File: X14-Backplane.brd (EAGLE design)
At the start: 88.9 x 139.7 mm, 34 parts, among them J2 PXC-PTSM-04-RA-1778641, J3 PXC-8-RA-1778683, J8 PXC-8-RA-1778683

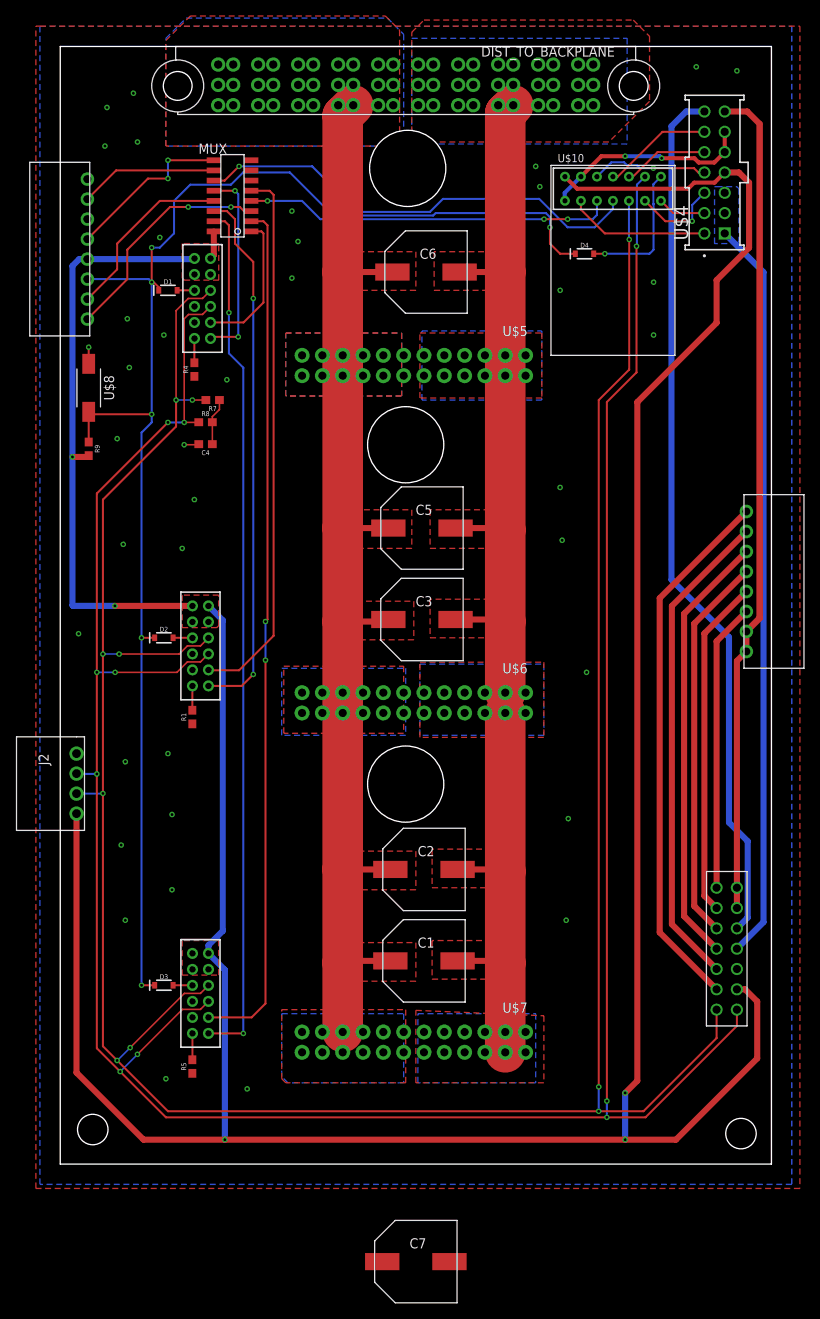
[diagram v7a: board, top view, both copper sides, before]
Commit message: Added Silkscreen, last cap
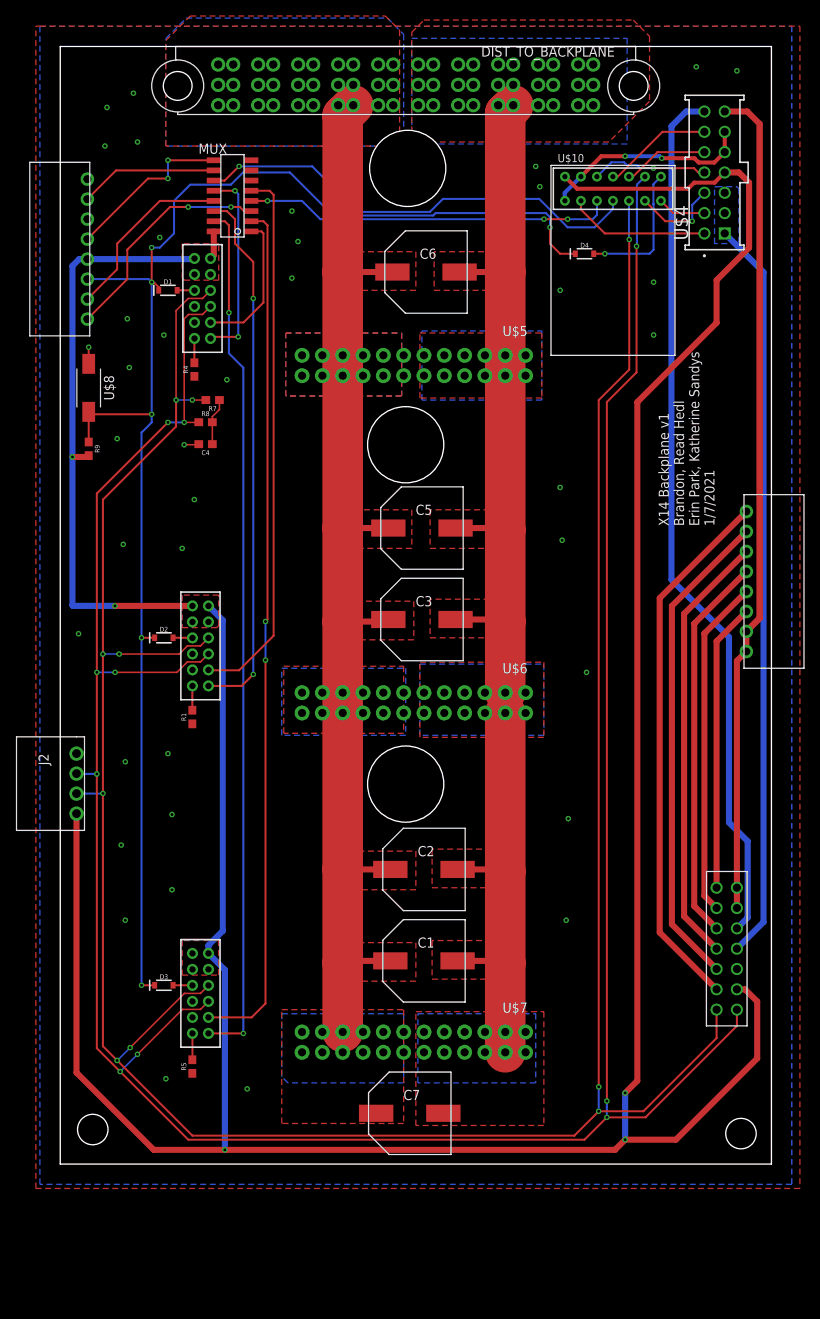
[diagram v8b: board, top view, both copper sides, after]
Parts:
- moved C7 18.6 mm to (43.7, 6.35)
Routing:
- net CAN_H: track 340.3 -> 342.8 mm
- net 3V3: track 434.3 -> 436.6 mm
- net CAN_L: track 344.7 -> 347.0 mm
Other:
- board text added: "X14 Backplane v1 Brandon, Read Hedl Erin Park, Katherine Sandys 1/7/2021"
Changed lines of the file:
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@@
 <hole x="43.18" y="89.916" drill="9.525"/>
 <hole x="43.434" y="124.46" drill="9.525"/>
+<text x="81.788" y="79.756" size="1.27" layer="25" rot="R90">X14 Backplane v1
+Brandon, Read Hedl
+Erin Park, Katherine Sandys
+1/7/2021</text>
 </plain>
 <attributes>
@@
 <attribute name="VALUE" x="45.72" y="108.966" size="1.27" layer="27" align="center"/>
 </element>
-<element name="C7" library="CAP, aluminin-capacitor-brick-UCM1H331MNL1GS" package="CAPAE1030X1050N" package3d_urn="urn:adsk.eagle:package:24202090/2" value="330uF" x="44.45" y="-12.192" smashed="yes">
-<attribute name="ARROW_PART_NUMBER" value="UCM1H331MNL1GS" x="44.45" y="-12.192" size="1.778" layer="27" display="off"/>
-<attribute name="ARROW_PRICE-STOCK" value="https://www.arrow.com/en/products/ucm1h331mnl1gs/nichicon" x="44.45" y="-12.192" size="1.778" layer="27" display="off"/>
-<attribute name="DESCRIPTION" value="Nichicon 330uF 50 V Aluminium Electrolytic Capacitor SMD, CM Series 2000h 10 (Dia.) x 10mm" x="44.45" y="-12.192" size="1.778" layer="27" display="off"/>
-<attribute name="HEIGHT" value="10.5mm" x="44.45" y="-12.192" size="1.778" layer="27" display="off"/>
-<attribute name="MANUFACTURER_NAME" value="Nichicon" x="44.45" y="-12.192" size="1.778" layer="27" display="off"/>
-<attribute name="MANUFACTURER_PART_NUMBER" value="UCM1H331MNL1GS" x="44.45" y="-12.192" size="1.778" layer="27" display="off"/>
-<attribute name="MOUSER_PART_NUMBER" value="647-UCM1H331MNL1GS" x="44.45" y="-12.192" size="1.778" layer="27" display="off"/>
-<attribute name="MOUSER_PRICE-STOCK" value="https://www.mouser.co.uk/ProductDetail/Nichicon/UCM1H331MNL1GS?qs=DSgADHjnLTkTovFLdbC%252BNg%3D%3D" x="44.45" y="-12.192" size="1.778" layer="27" display="off"/>
-<attribute name="NAME" x="44.704" y="-9.906" size="1.27" layer="25" align="center"/>
-<attribute name="VALUE" x="44.45" y="-14.732" size="1.27" layer="27" align="center"/>
+<element name="C7" library="CAP, aluminin-capacitor-brick-UCM1H331MNL1GS" package="CAPAE1030X1050N" package3d_urn="urn:adsk.eagle:package:24202090/2" value="330uF" x="43.688" y="6.35" smashed="yes">
+<attribute name="ARROW_PART_NUMBER" value="UCM1H331MNL1GS" x="43.688" y="6.35" size="1.778" layer="27" display="off"/>
+<attribute name="ARROW_PRICE-STOCK" value="https://www.arrow.com/en/products/ucm1h331mnl1gs/nichicon" x="43.688" y="6.35" size="1.778" layer="27" display="off"/>
+<attribute name="DESCRIPTION" value="Nichicon 330uF 50 V Aluminium Electrolytic Capacitor SMD, CM Series 2000h 10 (Dia.) x 10mm" x="43.688" y="6.35" size="1.778" layer="27" display="off"/>
+<attribute name="HEIGHT" value="10.5mm" x="43.688" y="6.35" size="1.778" layer="27" display="off"/>
+<attribute name="MANUFACTURER_NAME" value="Nichicon" x="43.688" y="6.35" size="1.778" layer="27" display="off"/>
+<attribute name="MANUFACTURER_PART_NUMBER" value="UCM1H331MNL1GS" x="43.688" y="6.35" size="1.778" layer="27" display="off"/>
+<attribute name="MOUSER_PART_NUMBER" value="647-UCM1H331MNL1GS" x="43.688" y="6.35" size="1.778" layer="27" display="off"/>
+<attribute name="MOUSER_PRICE-STOCK" value="https://www.mouser.co.uk/ProductDetail/Nichicon/UCM1H331MNL1GS?qs=DSgADHjnLTkTovFLdbC%252BNg%3D%3D" x="43.688" y="6.35" size="1.778" layer="27" display="off"/>
+<attribute name="NAME" x="43.942" y="8.636" size="1.27" layer="25" align="center"/>
+<attribute name="VALUE" x="43.688" y="3.81" size="1.27" layer="27" align="center"/>
 </element>
 </elements>
@@
 <wire x1="82.042" y1="15.748" x2="72.898" y2="6.604" width="0.254" layer="1"/>
 <wire x1="72.898" y1="6.604" x2="67.31" y2="6.604" width="0.254" layer="1"/>
-<wire x1="67.31" y1="6.604" x2="13.462" y2="6.604" width="0.254" layer="1"/>
-<wire x1="13.462" y1="6.604" x2="7.112" y2="12.954" width="0.254" layer="1"/>
+<wire x1="67.31" y1="6.604" x2="64.262" y2="3.556" width="0.254" layer="1"/>
+<wire x1="64.262" y1="3.556" x2="16.51" y2="3.556" width="0.254" layer="1"/>
+<wire x1="16.51" y1="3.556" x2="7.112" y2="12.954" width="0.254" layer="1"/>
 <wire x1="7.112" y1="12.954" x2="5.334" y2="14.732" width="0.254" layer="1"/>
 <wire x1="17.526" y1="21.336" x2="18.526" y2="22.336" width="0.2032" layer="1"/>
@@
 <wire x1="84.582" y1="19.304" x2="84.582" y2="17.272" width="0.254" layer="1"/>
 <wire x1="84.582" y1="17.272" x2="73.152" y2="5.842" width="0.254" layer="1"/>
-<wire x1="13.208" y1="5.842" x2="7.493" y2="11.557" width="0.254" layer="1"/>
+<wire x1="16.002" y1="3.048" x2="7.493" y2="11.557" width="0.254" layer="1"/>
 <wire x1="7.493" y1="11.557" x2="4.572" y2="14.478" width="0.254" layer="1"/>
 <wire x1="73.152" y1="5.842" x2="68.326" y2="5.842" width="0.254" layer="1"/>
-<wire x1="68.326" y1="5.842" x2="13.208" y2="5.842" width="0.254" layer="1"/>
+<wire x1="68.326" y1="5.842" x2="65.532" y2="3.048" width="0.254" layer="1"/>
+<wire x1="65.532" y1="3.048" x2="16.002" y2="3.048" width="0.254" layer="1"/>
 <wire x1="18.526" y1="20.336" x2="17.5258" y2="19.3358" width="0.2032" layer="1"/>
 <wire x1="15.2718" y1="19.3358" x2="9.652" y2="13.716" width="0.2032" layer="1"/>
@@
 <polygon width="1.016" layer="1" isolate="0.508">
 <vertex x="27.686" y="19.304"/>
-<vertex x="43.18" y="19.304"/>
-<vertex x="43.18" y="10.16"/>
-<vertex x="28.194" y="10.16"/>
-<vertex x="27.686" y="10.668"/>
+<vertex x="42.926" y="19.304"/>
+<vertex x="42.926" y="5.08"/>
+<vertex x="27.686" y="5.08"/>
 </polygon>
 <polygon width="1.016" layer="16" isolate="0.508">
@@
 <vertex x="35.56" y="76.962"/>
 </polygon>
-<wire x1="40.386" y1="13.97" x2="40.25" y2="-12.192" width="0" layer="19" extent="1-1"/>
 </signal>
 <signal name="SWCLK_IN">
@@
 </polygon>
 <polygon width="1.016" layer="1" isolate="0.508" rank="2">
-<vertex x="44.45" y="19.215303125"/>
-<vertex x="60.452" y="18.537971875"/>
-<vertex x="60.452" y="10.16"/>
-<vertex x="44.45" y="10.16"/>
+<vertex x="44.45" y="19.05"/>
+<vertex x="60.452" y="19.05"/>
+<vertex x="60.452" y="4.826"/>
+<vertex x="44.45" y="4.826"/>
 </polygon>
 <polygon width="1.016" layer="16" isolate="0.508" rank="2">
@@
 <vertex x="54.864" y="81.788"/>
 </polygon>
-<wire x1="48.006" y1="13.97" x2="48.65" y2="-12.192" width="0" layer="19" extent="1-1"/>
 </signal>
 <signal name="N$3">
@@
 <vertex x="19.812" y="27.94"/>
 </polygon>
-<wire x1="70.612" y1="3.048" x2="20.574" y2="3.048" width="0.762" layer="1"/>
-<wire x1="20.574" y1="3.048" x2="10.414" y2="3.048" width="0.762" layer="1"/>
+<wire x1="70.612" y1="3.048" x2="69.342" y2="1.778" width="0.762" layer="1"/>
+<wire x1="69.342" y1="1.778" x2="20.574" y2="1.778" width="0.762" layer="1"/>
+<wire x1="20.574" y1="1.778" x2="11.684" y2="1.778" width="0.762" layer="1"/>
 <wire x1="1.524" y1="112.268" x2="1.524" y2="88.392" width="0.762" layer="16"/>
 <wire x1="1.524" y1="88.392" x2="1.524" y2="69.85" width="0.762" layer="16"/>
@@
 <wire x1="6.8326" y1="69.7738" x2="1.6002" y2="69.7738" width="0.762" layer="16"/>
 <wire x1="1.6002" y1="69.7738" x2="1.524" y2="69.85" width="0.762" layer="16"/>
-<wire x1="10.414" y1="3.048" x2="2.032" y2="11.43" width="0.762" layer="1"/>
+<wire x1="11.684" y1="1.778" x2="2.032" y2="11.43" width="0.762" layer="1"/>
 <wire x1="2.032" y1="11.43" x2="2.032" y2="43.808" width="0.762" layer="1"/>
-<via x="20.574" y="3.048" extent="1-16" drill="0.35"/>
-<wire x1="20.574" y1="3.048" x2="20.574" y2="24.288" width="0.762" layer="16"/>
+<via x="20.574" y="1.778" extent="1-16" drill="0.35"/>
+<wire x1="20.574" y1="1.778" x2="20.574" y2="24.288" width="0.762" layer="16"/>
 <wire x1="20.574" y1="24.288" x2="18.526" y2="26.336" width="0.762" layer="16"/>
 <wire x1="20.32" y1="67.976" x2="20.32" y2="29.146" width="0.762" layer="16"/>
@@
 </drawing>
 <compatibility>
+<note version="6.3" minversion="6.2.2" severity="warning">
+Since Version 6.2.2 text objects can contain more than one line,
+which will not be processed correctly with this version.
+</note>
 <note version="8.2" severity="warning">
 Since Version 8.2, EAGLE supports online libraries. The ids
